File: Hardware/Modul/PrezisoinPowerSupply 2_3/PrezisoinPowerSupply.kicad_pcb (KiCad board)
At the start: 4 copper layers, 91 x 100 mm, 229 parts, among them J1 Supply, J2 Conn_01x03_Pin, J3 Conn_02x05_Odd_Even, J6 Output, J7 USB_C_Receptacle, J8 Conn_01x08_Socket, K1 EE2-5NU, K3 SANYOU_SRD_Form_C, Q1 IRFP240, Q2 IRFP9240, Q3 MMBT3904, Q4 IRFP9240, Q5 MMBT3904, Q6 MMBT3904, Q7 MMBT3904, Q8 MMBT3904, Q9 IRFP240, U1 AP63200WU, U10 OPA4189, U11 OPA4189, U12 OPA189, U13 TME-1212S, U14 LM7805_TO220, U15 OPA2192, U16 ATtiny3227-M, U17 TS5A23159RSE, U18 LM7812_TO220, U19 TLV9301xDBV, U2 DG469, U20 ICM7555xB, U21 ADS1219, U3 ADA4522, U4 CPC1017N, U5 ISO7763FDBQ, U6 CH340C, U7 DAC8564C/D, U8 MCP9700Ax-ETT, U9 MCP9700Ax-ETT

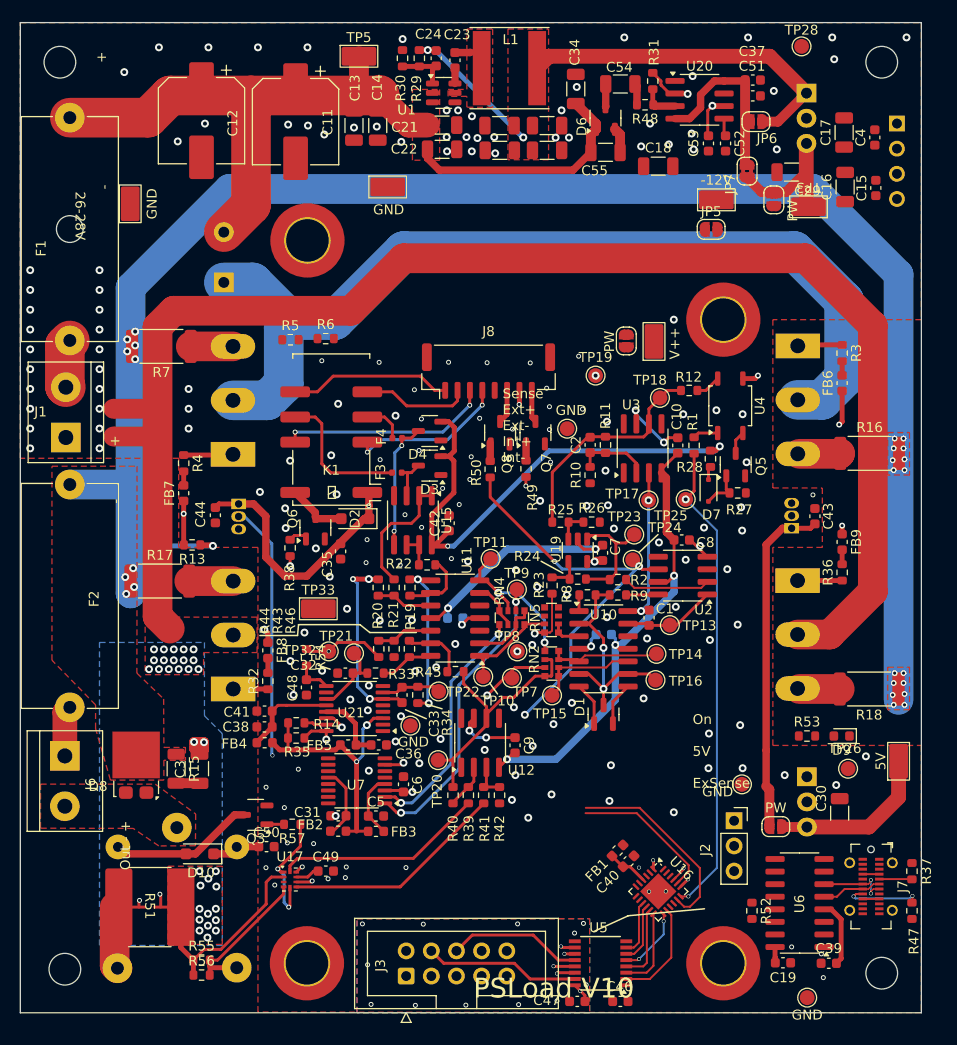
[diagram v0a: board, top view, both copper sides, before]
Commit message: hardware Fet Range switching
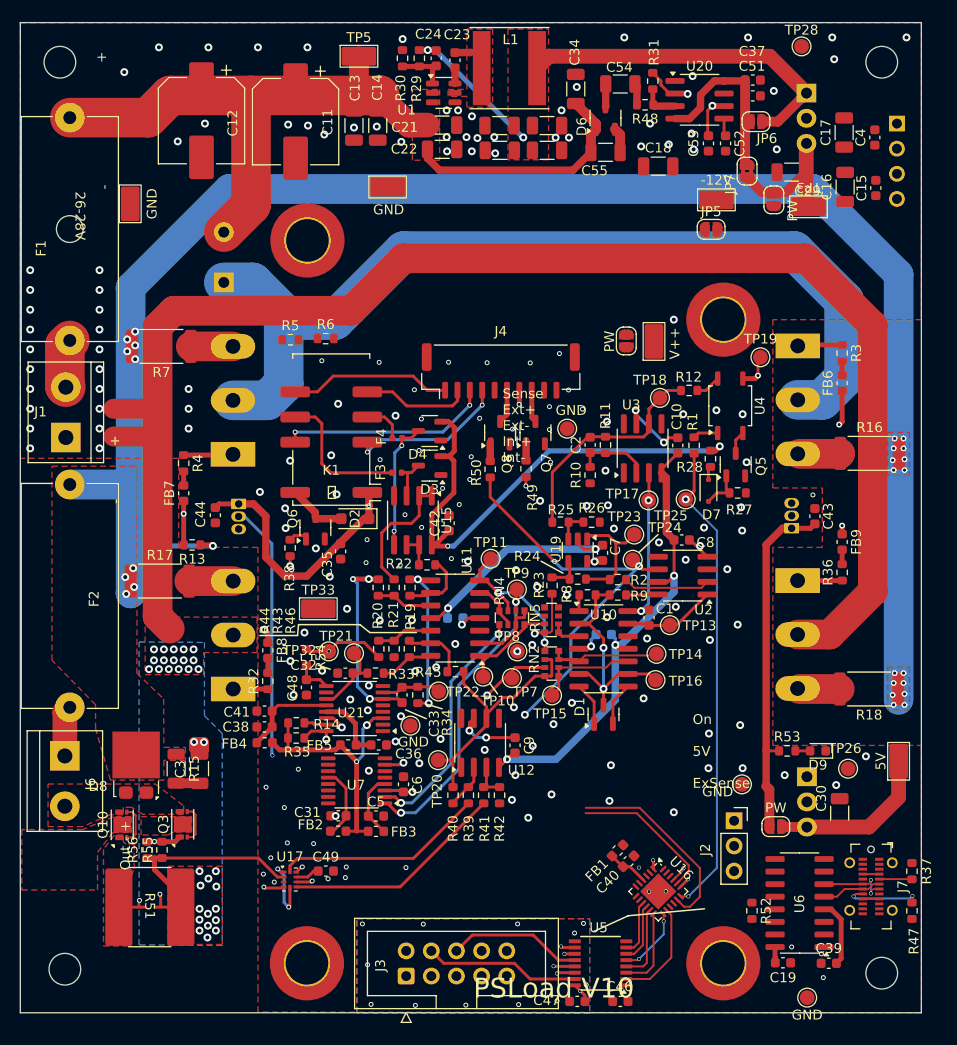
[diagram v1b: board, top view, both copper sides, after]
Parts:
- removed C50: 100n, Capacitor_SMD:C_0603_1608Metric
- removed D10: 1N4007, Diode_SMD:D_SOD-123F
- removed J8: Conn_01x08_Socket, Connector_JST:JST_GH_BM08B-GHS-TBT_1x08-1MP_P1.25mm_Vertical
- removed K3: SANYOU_SRD_Form_C, Relay_THT:Relay_SPDT_SANYOU_SRD_Series_Form_C
- removed R57: 1k, Resistor_SMD:R_0603_1608Metric
- added J4: Conn_01x10_Socket, Connector_JST:JST_GH_BM10B-GHS-TBT_1x10-1MP_P1.25mm_Vertical, F.Cu at (144.5, 85.2)
- added Q10: DMN2008, Library:DFN-6-1EP_3x2mm_P0.5mm_EP1.65x1.35mm bearb, F.Cu at (106.3, 131.0)
- Q3: value MMBT3904 -> DMN2008; footprint Package_TO_SOT_SMD:SOT-23-3 -> Library:DFN-6-1EP_3x2mm_P0.5mm_EP1.65x1.35mm bearb
- R5, R6: value 1k -> 100k
- moved TP19 16.8 mm to (170.8, 83.8)
- moved R56 13.8 mm to (108.8, 133.6), turned to 90 degrees
- moved R55 11.8 mm to (110.3, 133.6), turned to 90 degrees
- moved Q3 7.42 mm to (112.4, 131.0), turned to 0 degrees
- moved D9 2.83 mm to (176.6, 123.5)
- moved R53 2.50 mm to (173.4, 123.5)
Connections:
- Q3 pad 1: Net-(Q3-B) -> Net-(Q3-D1-Pad1)
- Q3 pad 3: Net-(D10-A) -> Net-(Q3-G1-Pad3)
- R51 pad 1: Net-(K3-Pad4) -> /5A Shunt Hi
- R55 pad 2: Net-(K3-Pad3) -> Net-(Q3-D1-Pad1)
- R56 pad 2: Net-(K3-Pad3) -> Net-(Q3-D1-Pad1)
- U17 pad 4: Net-(K3-Pad3) -> Net-(Q3-D1-Pad1)
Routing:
- net Net-(Q3-D1-Pad1): track 0.00 -> 18.6 mm, vias 0 -> 2
- net Net-(K3-Pad3): track 15.2 -> 0.00 mm
- net Net-(D10-A): track 14.8 -> 0.00 mm
- net Net-(K3-Pad4): track 6.29 -> 0.00 mm
- net RangeSW: track 12.5 -> 7.03 mm
- net +12V: track 67.6 -> 62.8 mm
- net Net-(Q10-G1-Pad3): track 0.00 -> 3.98 mm
- net Net-(Q3-G1-Pad3): track 0.00 -> 3.90 mm
- net Net-(FB6-Pad1): track 116.6 -> 118.6 mm, vias 6 -> 5
- net Net-(Q3-B): track 1.73 -> 0.00 mm
- net Net-(D9-A): track 0.00 -> 1.49 mm
- net +5V: track 113.3 -> 114.7 mm
- net GNDPWR: track 170.3 -> 169.6 mm
- net GND: vias 187 -> 188
- added copper zone on F.Cu, net /5A Shunt Hi
- added copper zone on F.Cu, net /HeatSink1
- added copper zone on F.Cu, net /HeatSink2

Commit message: rooting and new frontDist
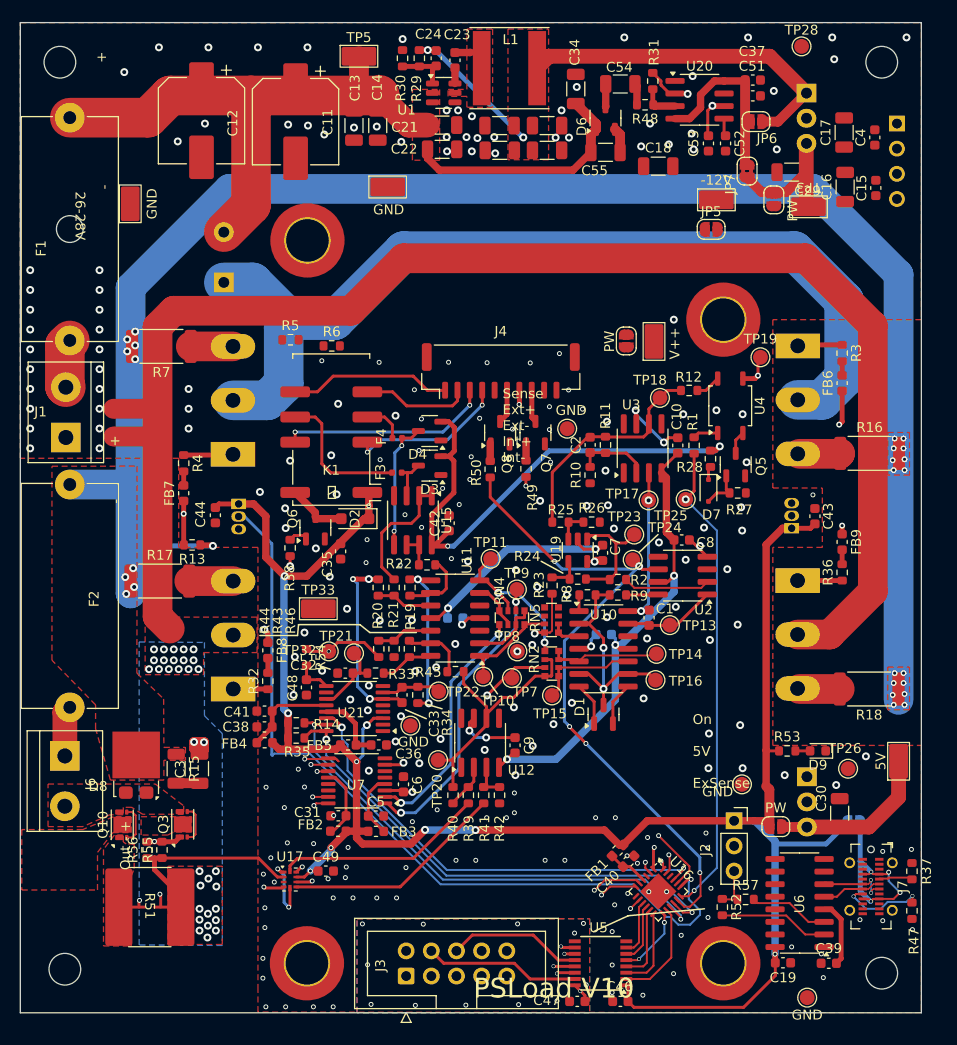
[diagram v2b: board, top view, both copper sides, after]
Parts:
- added JP2: USB PW Link, Jumper:SolderJumper-2_P1.3mm_Open_RoundedPad1.0x1.5mm, B.Cu at (180.2, 130.8)
- added R57: 100, Resistor_SMD:R_0603_1608Metric, F.Cu at (169.2, 138.6)
- moved R52 3.01 mm to (166.9, 139.3)
- moved R6 0.96 mm to (127.5, 82.7)
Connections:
- U6 pad 3: UPDI -> Net-(U6-RXD)
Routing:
- net +5V: track 114.7 -> 245.8 mm, vias 4 -> 11
- net SDA: track 2.28 -> 50.9 mm, vias 0 -> 2
- net SCL: track 3.35 -> 50.9 mm, vias 1 -> 2
- net DAC Sync: track 0.00 -> 46.1 mm, vias 0 -> 2
- net SCK: track 0.00 -> 41.4 mm, vias 0 -> 2
- net MoSi: track 0.00 -> 40.5 mm, vias 0 -> 2
- net DAC Enable: track 0.00 -> 40.5 mm, vias 0 -> 2
- net DAC LDAC: track 0.00 -> 38.5 mm, vias 0 -> 2
- net Net-(JP2-A): track 3.34 -> 19.6 mm, vias 0 -> 4
- net UPDI: track 0.00 -> 13.8 mm, vias 0 -> 1
- net Net-(U6-TXD): track 0.00 -> 11.1 mm
- net Net-(U6-RXD): track 0.00 -> 8.04 mm
- net TempData#1: track 74.6 -> 82.2 mm, vias 2 -> 1
- net ON: track 62.9 -> 68.4 mm, vias 3 -> 5
- net SensSW: track 81.6 -> 86.9 mm, vias 2 -> 3
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
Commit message: finalise rooting
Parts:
- added C50: 100n, Capacitor_SMD:C_0603_1608Metric, F.Cu at (185.0, 131.2)
- added C56: 100n, Capacitor_SMD:C_0603_1608Metric, F.Cu at (119.7, 129.8)
- added U22: SN74LVC1G14DBV, Package_TO_SOT_SMD:SOT-23-5, F.Cu at (116.8, 129.8)
- moved R6 11.1 mm to (120.1, 91.0)
- moved TP4 6.92 mm to (154.5, 78.0)
- moved J6 4.93 mm to (100.5, 129.0), turned to 90 degrees
- moved R5 4.56 mm to (120.1, 85.3)
- moved TP6 4.45 mm to (169.4, 71.1)
- moved TP1 2.73 mm to (109.5, 67.0), turned to 180 degrees
- moved C18 2.60 mm to (158.1, 65.5)
- moved C16 0.91 mm to (180.2, 66.8)
- moved C15 0.74 mm to (182.7, 66.0)
- moved FB7 0.70 mm to (113.2, 97.5)
- moved R4 0.70 mm to (113.2, 94.5)
- moved R13 0.65 mm to (114.0, 102.8)
- moved REF** 0.64 mm to (100.0, 146.0)
- moved JP5 0.12 mm to (165.7, 70.9), turned to 180 degrees
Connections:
- F2 pad 2: Net-(J6-Pin_1) -> Net-(J6-Pin_2)
- J6 pad 1: Net-(J6-Pin_1) -> /outLOW
- J6 pad 2: /outLOW -> Net-(J6-Pin_2)
- Q3 pad 3: Net-(Q3-G1-Pad3) -> RangeSW
- Q3 pad 6: Net-(Q3-G1-Pad3) -> RangeSW
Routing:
- net GND: track 1.10 -> 94.5 mm, vias 227 -> 148
- net /outLOW: track 0.00 -> 49.2 mm, vias 0 -> 1
- net +12V: track 62.8 -> 108.2 mm, vias 6 -> 8
- net -12V: track 84.6 -> 122.2 mm, vias 5 -> 9
- net +VDC: track 135.3 -> 164.5 mm, vias 2 -> 4
- net /buckConLDO/12V: track 119.8 -> 95.3 mm
- net /buckConLDO/-12V: track 0.00 -> 22.1 mm
- net /buckConLDO/..36V: track 2.54 -> 24.6 mm, vias 0 -> 2
- net RangeSW: track 7.03 -> 25.5 mm
- net Net-(Q10-G1-Pad3): track 3.98 -> 15.4 mm, vias 0 -> 2
- net Net-(F4-Pad2): track 4.20 -> 14.9 mm, vias 0 -> 2
- net /outHi: track 175.6 -> 186.1 mm, vias 26 -> 27
- net +5V: track 245.8 -> 254.4 mm
- net Net-(F3-Pad2): track 14.5 -> 21.3 mm
- net +36V: track 7.43 -> 14.2 mm
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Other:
- board text removed: "On 5V ExSense"
- board text removed: "Sense Ext+ Ext- Int+ Int-"

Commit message: hardware ####
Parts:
- moved R13 1.44 mm to (113.2, 101.5), turned to 90 degrees
